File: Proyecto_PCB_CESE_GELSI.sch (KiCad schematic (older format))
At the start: 19 parts, among them IC1 SC2272L4, IC2 ASM1117-33, IC3 SN74LVC1G125DCKR, IC4 H5V3G

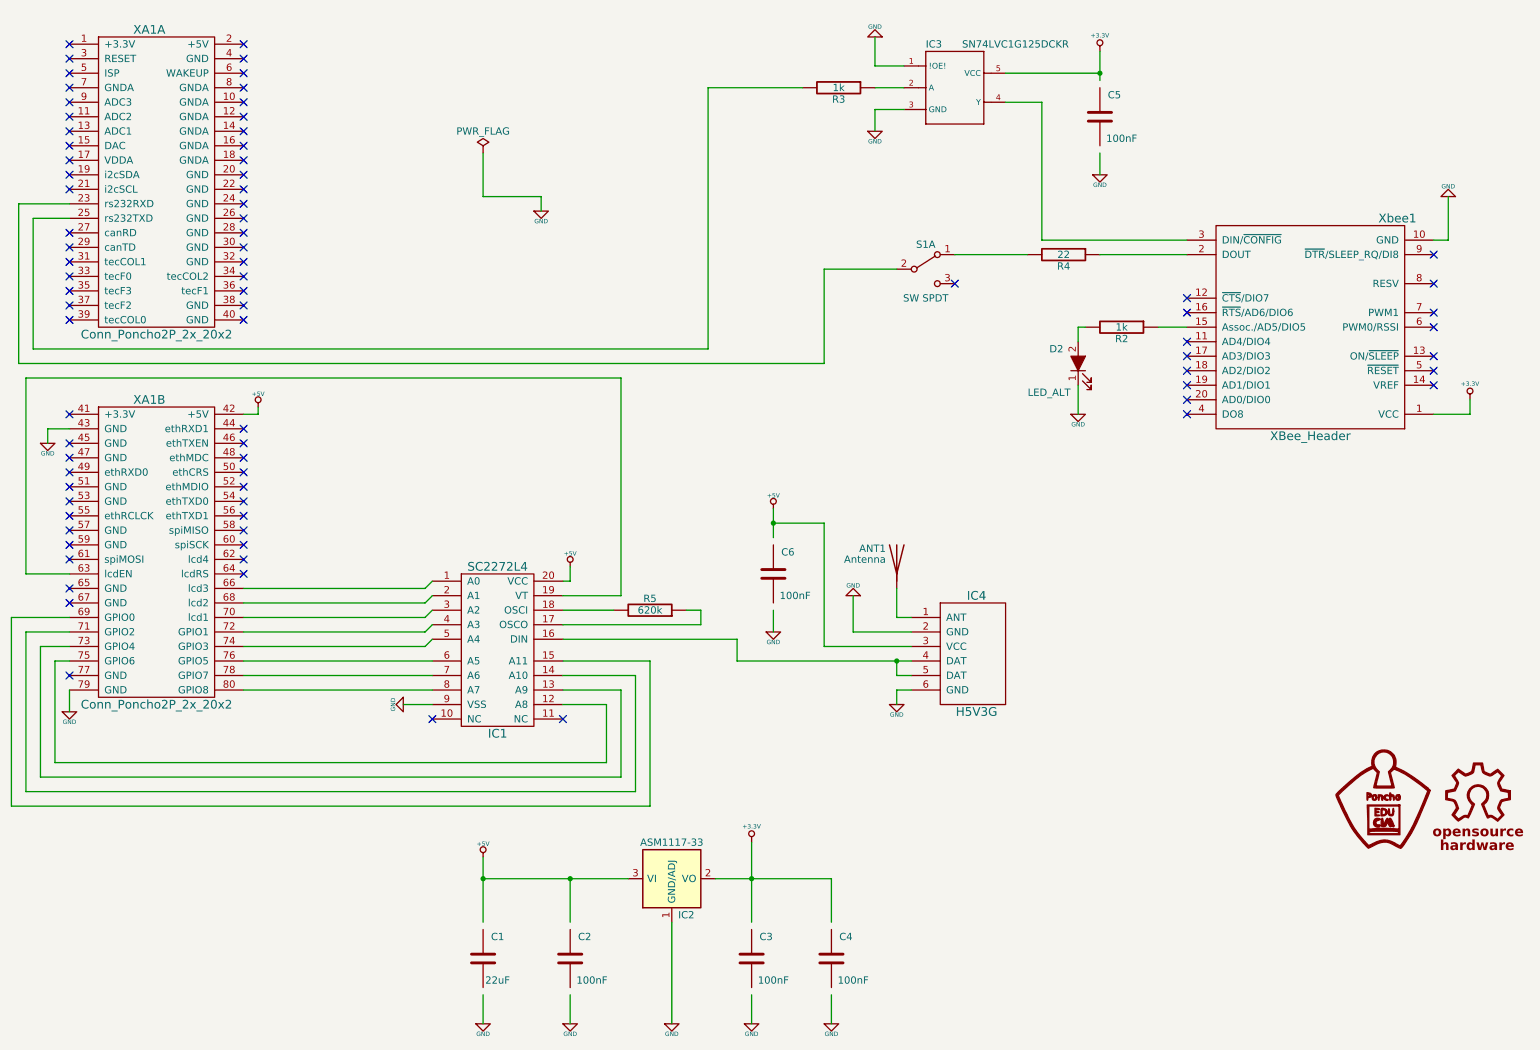
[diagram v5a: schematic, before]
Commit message: Correciones totales al esquemático, pcb y organización parcial en visor 3D
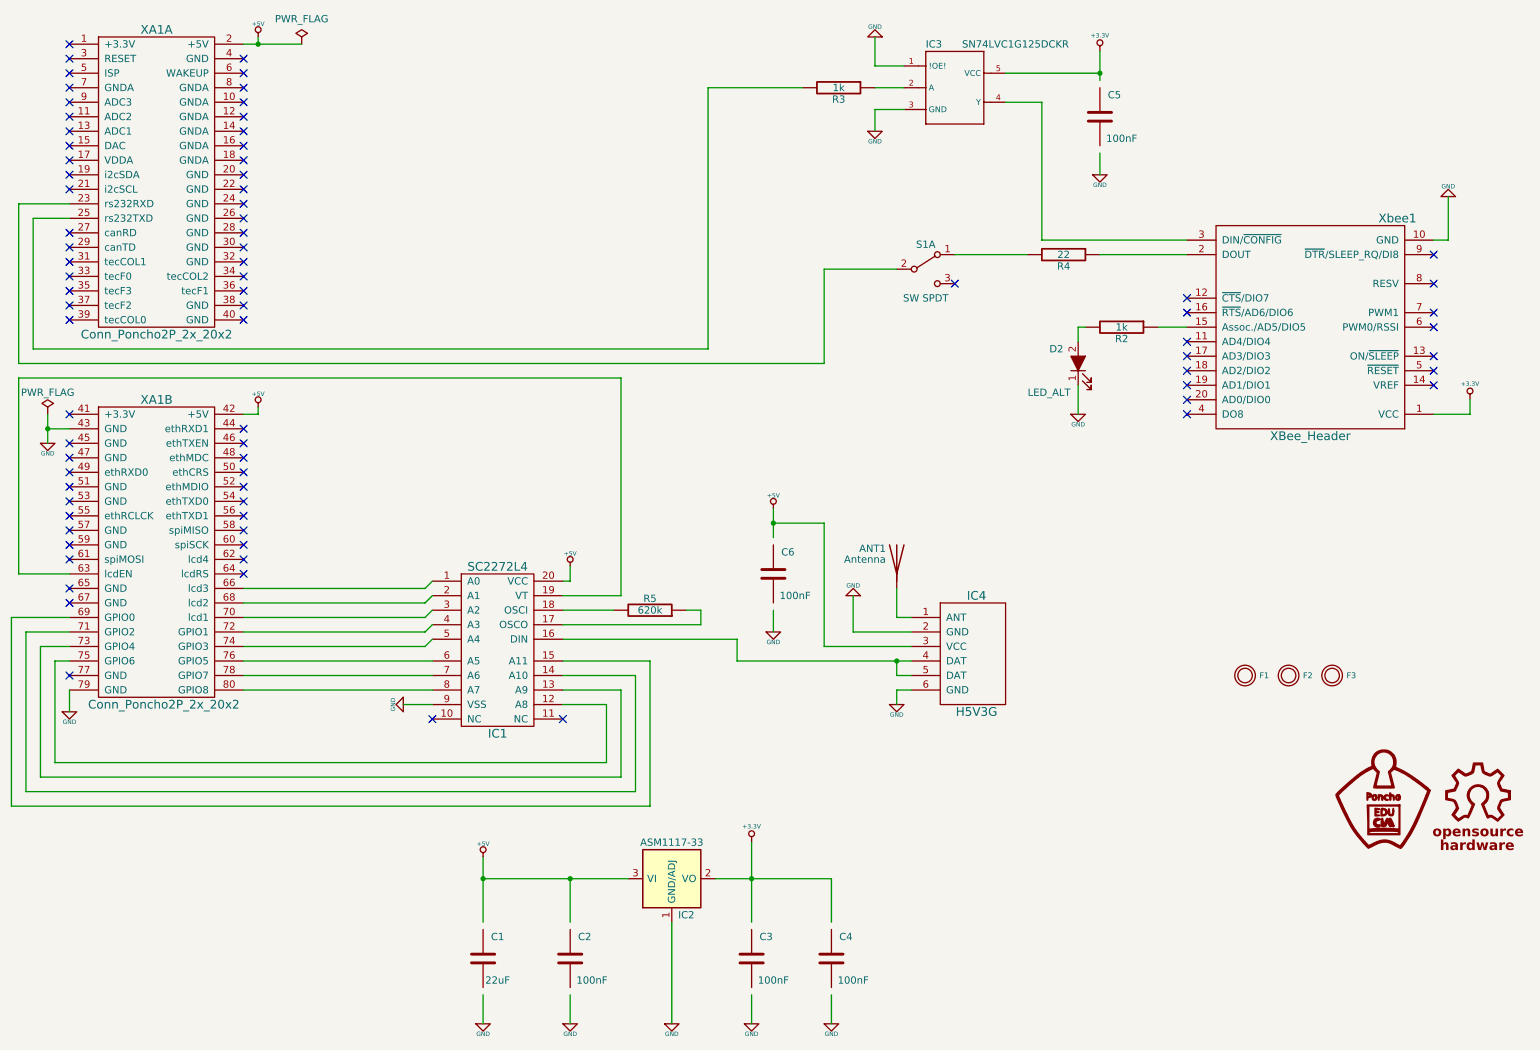
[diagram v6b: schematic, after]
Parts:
- added F1, F2, F3: FIDUCIAL, projectHuellas:Fiducial_1mm, symbol FIDUCIAL
- C1, C2, C3, C4, C5, C6: footprint projectHuellas:C_0603_HandSoldering -> projectHuellas:C_0805_HandSoldering
- R2, R3, R4, R5: footprint projectHuellas:R_1206_HandSoldering -> projectHuellas:R_0805_HandSoldering
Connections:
- wire segments 111 -> 110
- no-connect marks 80 -> 79

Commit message: Update final a producción.
Subida final de archivos para sustentar las cosas a corregir marcadas por el profesor. Faltantes no conseguidos en visión 3D.
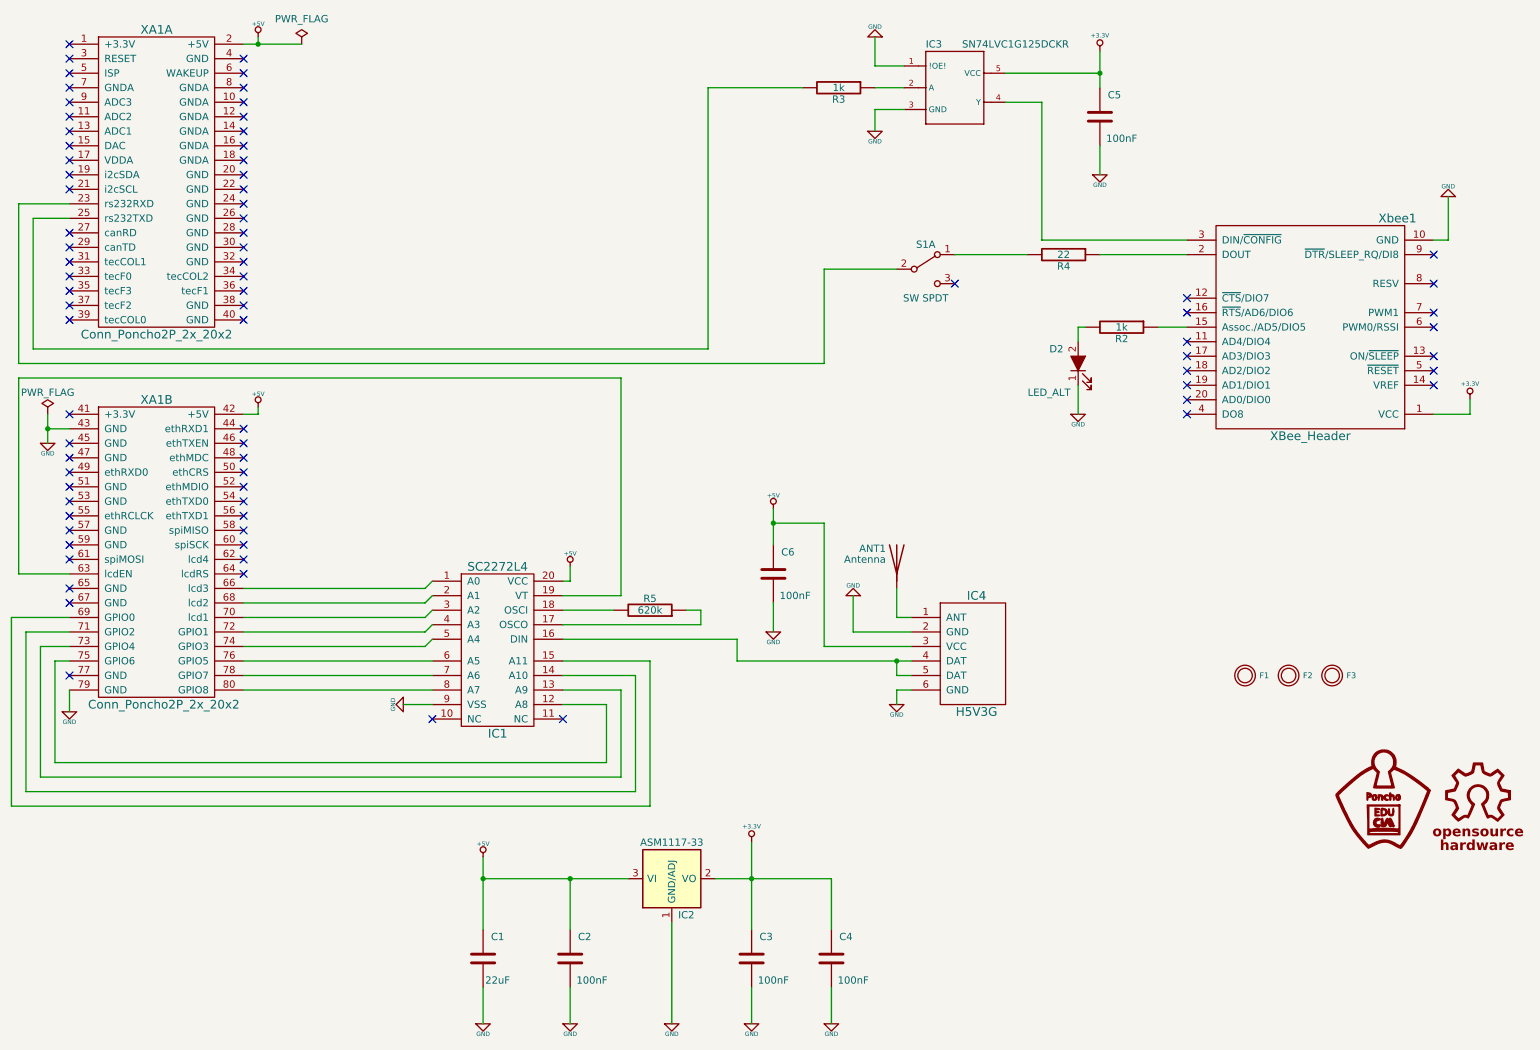
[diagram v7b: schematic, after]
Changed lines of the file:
@@
 LIBS:Poncho_Esqueleto
 LIBS:Misc_Poncho_Grande
-LIBS:ej2cese
 LIBS:Proyecto_PCB_CESE_GELSI-cache
-EELAYER 26 0
+EELAYER 25 0
 EELAYER END
 $Descr A4 11693 8268
@@
 $EndComp
 $Comp
-L +5V #PWR021
+L +5V #PWR019
 U 1 1 59619575
 P 4550 4400
-F 0 "#PWR021" H 4550 4490 20  0001 C CNN
+F 0 "#PWR019" H 4550 4490 20  0001 C CNN
 F 1 "+5V" H 4550 4490 30  0000 C CNN
 F 2 "" H 4550 4400 60  0001 C CNN
@@
 $EndComp
 $Comp
-L +3.3V #PWR022
+L +3.3V #PWR020
 U 1 1 596199FD
 P 10750 3250
-F 0 "#PWR022" H 10750 3210 30  0001 C CNN
+F 0 "#PWR020" H 10750 3210 30  0001 C CNN
 F 1 "+3.3V" H 10750 3360 30  0000 C CNN
 F 2 "" H 10750 3250 60  0001 C CNN
@@
 NoConn ~ 1100 3350
 $Comp
-L +5V #PWR023
+L +5V #PWR021
 U 1 1 5961AEFB
 P 2400 3300
-F 0 "#PWR023" H 2400 3390 20  0001 C CNN
+F 0 "#PWR021" H 2400 3390 20  0001 C CNN
 F 1 "+5V" H 2400 3390 30  0000 C CNN
 F 2 "" H 2400 3300 60  0000 C CNN
@@
 $EndComp
 $Comp
-L GND #PWR024
+L GND #PWR022
 U 1 1 596A4BCF
 P 950 3550
-F 0 "#PWR024" H 950 3550 30  0001 C CNN
+F 0 "#PWR022" H 950 3550 30  0001 C CNN
 F 1 "GND" H 950 3480 30  0000 C CNN
 F 2 "" H 950 3550 60  0001 C CNN
@@
 $EndComp
 $Comp
-L GND #PWR025
+L GND #PWR023
 U 1 1 596A4DA5
 P 1100 5400
-F 0 "#PWR025" H 1100 5400 30  0001 C CNN
+F 0 "#PWR023" H 1100 5400 30  0001 C CNN
 F 1 "GND" H 1100 5330 30  0000 C CNN
 F 2 "" H 1100 5400 60  0001 C CNN
@@
 $EndComp
 $Comp
-L PWR_FLAG #FLG01
+L PWR_FLAG #FLG024
 U 1 1 597CE502
 P 950 3350
-F 0 "#FLG01" H 950 3425 50  0001 C CNN
+F 0 "#FLG024" H 950 3425 50  0001 C CNN
 F 1 "PWR_FLAG" H 950 3500 50  0000 C CNN
 F 2 "" H 950 3350 50  0001 C CNN
@@
 $EndComp
 $Comp
-L +5V #PWR019
+L +5V #PWR025
 U 1 1 597CF26E
 P 2400 750
-F 0 "#PWR019" H 2400 840 20  0001 C CNN
+F 0 "#PWR025" H 2400 840 20  0001 C CNN
 F 1 "+5V" H 2400 840 30  0000 C CNN
 F 2 "" H 2400 750 60  0000 C CNN
@@
 $EndComp
 $Comp
-L PWR_FLAG #FLG02
+L PWR_FLAG #FLG026
 U 1 1 597D18BC
 P 2700 800
-F 0 "#FLG02" H 2700 875 50  0001 C CNN
+F 0 "#FLG026" H 2700 875 50  0001 C CNN
 F 1 "PWR_FLAG" H 2700 974 50  0000 C CNN
 F 2 "" H 2700 800 50  0001 C CNN
@@
 	6800 5250 6800 5350
 Wire Wire Line
-	5950 4700 5950 4850
-Wire Wire Line
-	6350 6550 6350 6850
-Wire Wire Line
-	4550 6550 4550 6850
-Wire Wire Line
-	3950 6400 3950 6850
-Wire Wire Line
-	3950 7350 3950 7550
-Wire Wire Line
-	4550 7350 4550 7550
-Wire Wire Line
-	5800 7350 5800 7550
-Wire Wire Line
-	6350 7350 6350 7550
+	5950 4650 5950 4850
+Wire Wire Line
+	6350 6550 6350 6900
+Wire Wire Line
+	4550 6550 4550 6900
+Wire Wire Line
+	3950 6400 3950 6900
+Wire Wire Line
+	3950 7300 3950 7550
+Wire Wire Line
+	4550 7300 4550 7550
+Wire Wire Line
+	5800 7300 5800 7550
+Wire Wire Line
+	6350 7300 6350 7550
 Wire Wire Line
 	5250 6850 5250 7550
@@
 	10600 2150 10600 1850
 Wire Wire Line
-	8200 1550 8200 1700
+	8200 1500 8200 1700
 Wire Wire Line
 	8800 2150 7800 2150
@@
 	4550 4500 4500 4500
 Wire Wire Line
-	5950 4000 5950 4200
+	5950 4000 5950 4250
 Connection ~ 5950 4100
 Wire Wire Line
@@
 	750  4450 1100 4450
 Wire Wire Line
-	5800 6300 5800 6850
+	5800 6300 5800 6900
 Wire Wire Line
 	5550 6550 6350 6550
@@
 	4550 4500 4550 4400
 Wire Wire Line
-	8200 1050 8200 850
+	8200 850  8200 1100
 Wire Wire Line
 	7550 1000 8200 1000
